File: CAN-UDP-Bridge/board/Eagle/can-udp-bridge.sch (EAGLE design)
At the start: 19 parts, among them IC1 MCP1703DB, IC2 MCP1703DB, Q1 16M, X1 B4B-ZR

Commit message: Added files via upload
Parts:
- removed C4: 100n, rcl:C-EUC0805
- removed C7, C8: 1µ, rcl:C-EUC0805
- removed IC1: MCP1703DB, linear:MCP1703DB
- removed R1: 10kR, rcl:R-EU_R0805
- added U$3: ROF-78E5.0-0.5SMD, ROF-78XX:ROF-78E5.0-0.5SMD
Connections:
- removed net N$12: R1.1, U$1.~RESET
- net +18V: now also U$3.VIN; no longer C8.2, IC1.VI
- net +3V3: no longer R1.2
- net +5V: now also U$3.VOUT; no longer C4.2, C7.2, IC1.VO
- net GND: now also U$3.GND; no longer C4.1, C7.1, C8.1, IC1.GND
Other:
- moved on the sheet: C1, C2, C3, Q1

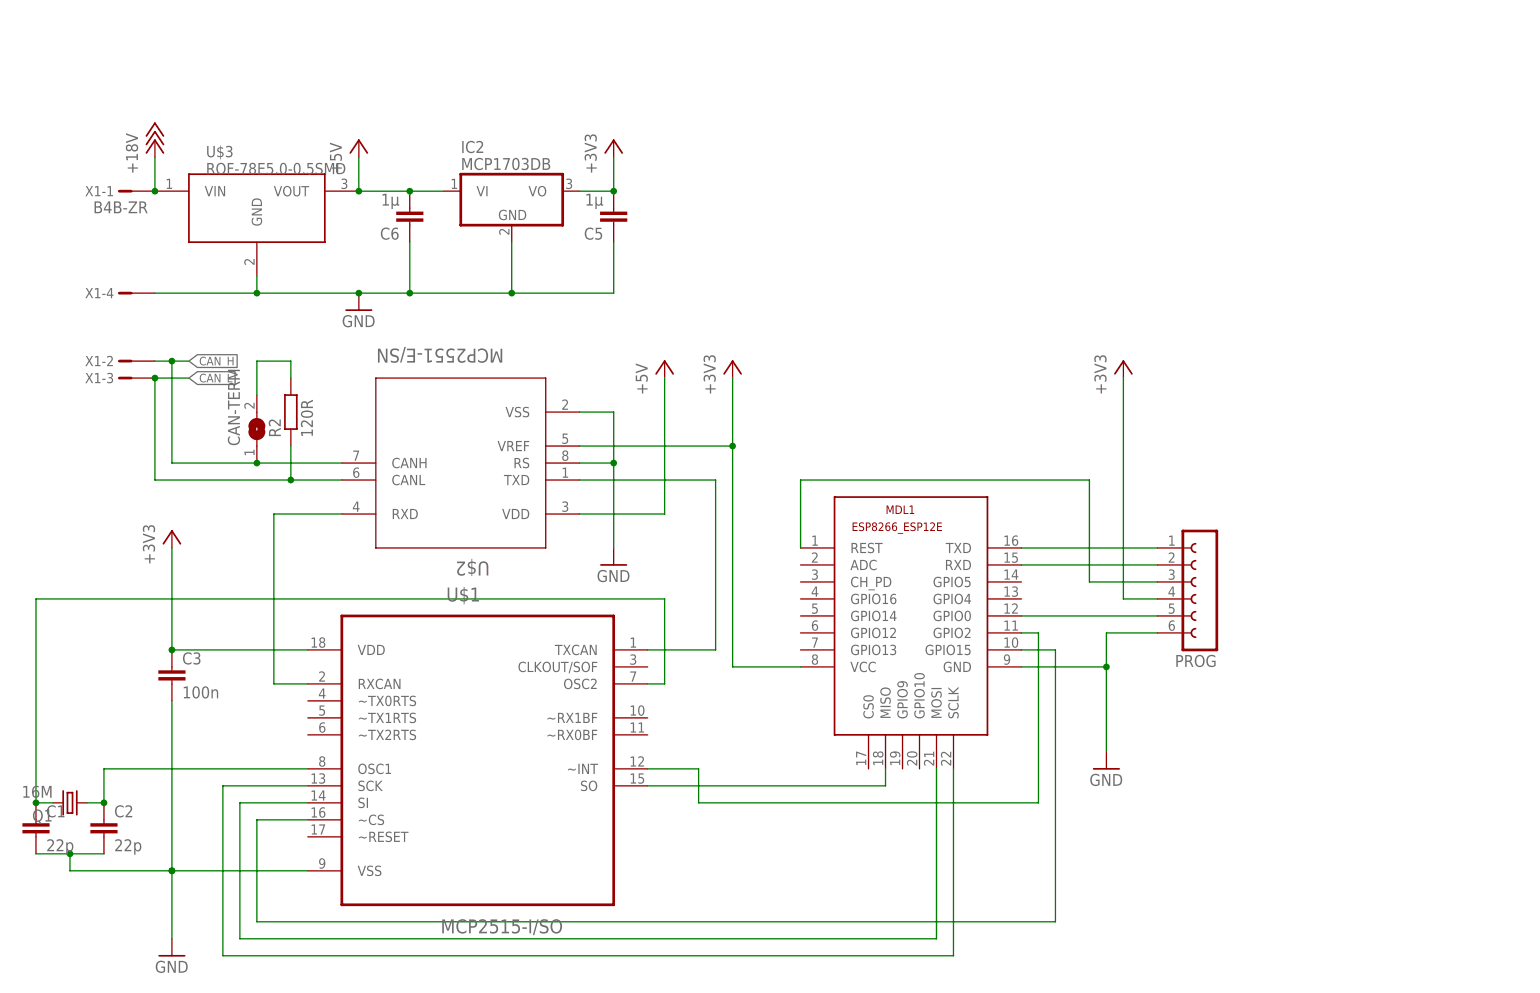
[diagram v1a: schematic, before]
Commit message: Schnittstelle angepasst an FT232RL.
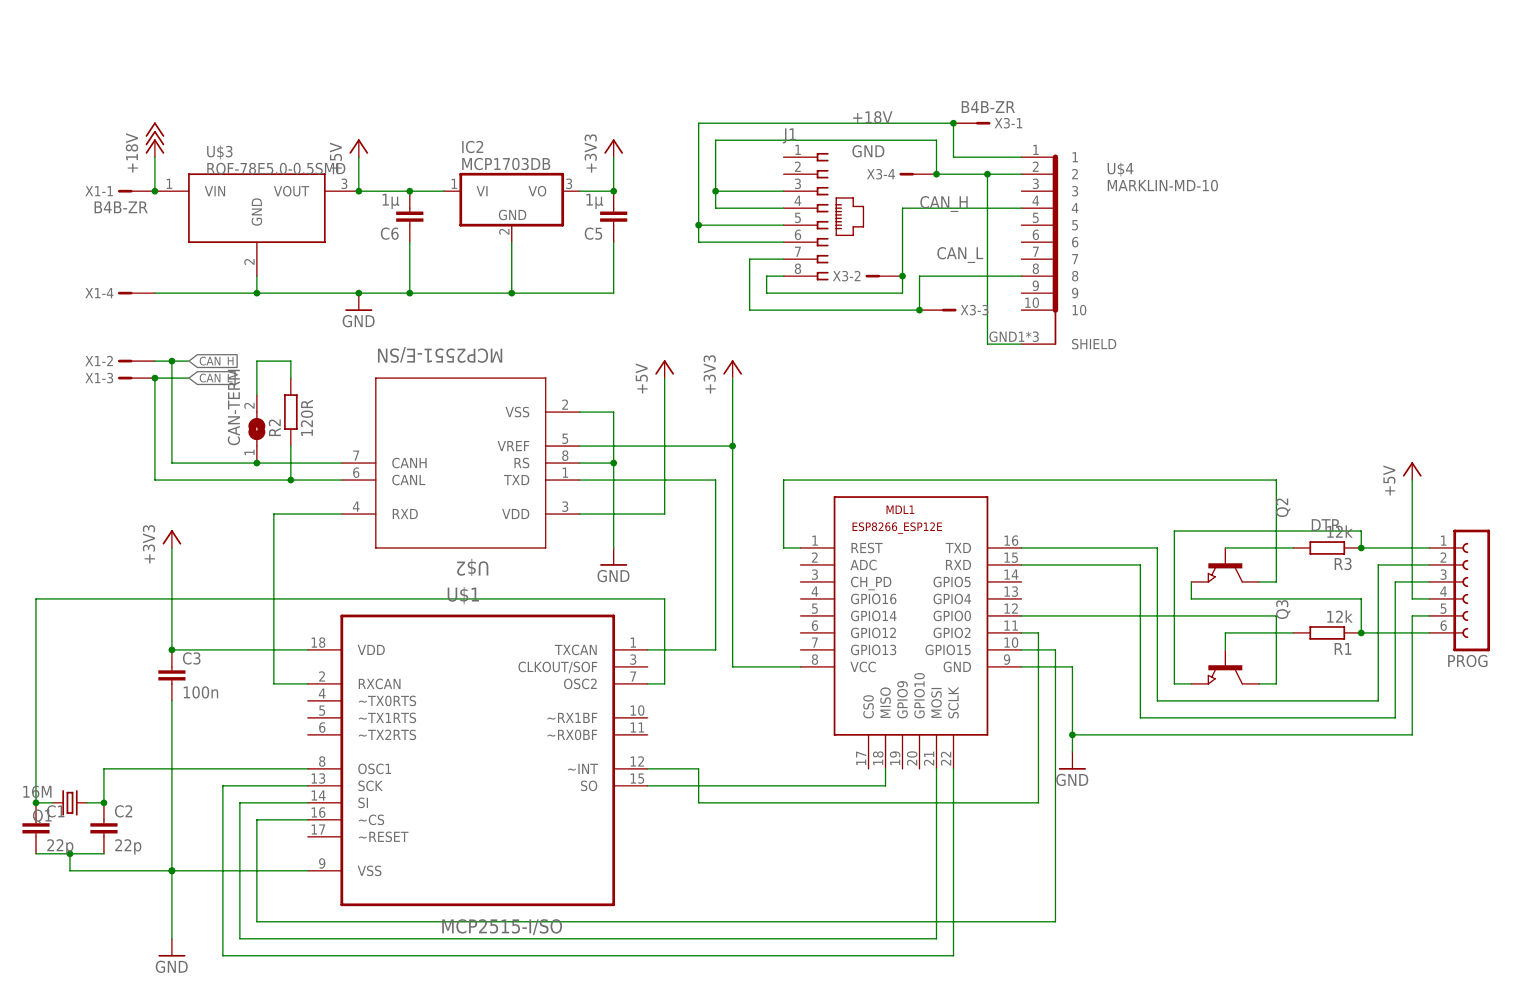
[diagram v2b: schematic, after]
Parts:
- added J1: (no value), con-amp:215877-7
- added Q2, Q3: (no value), semicon-smd-ipc:NPN-TRANSISTOR_SOT23
- added R1, R3: 12k, rcl:R-EU_R0805
- added U$4: MARKLIN-MD-10, Marklin-Mini-DIN:MARKLIN-MD-10
- added X3: B4B-ZR, con-jst:B4B-ZR
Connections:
- new net DTR: PROG.1, Q3.E, R3.1
- new net N$12: Q2.B, R3.2
- new net N$16: MDL1.TXD, PROG.2
- new net N$17: MDL1.RXD, PROG.3
- net +18V: now also J1.5, J1.6, U$4.1, X3-1.1
- net +3V3: no longer PROG.4
- net +5V: now also PROG.4
- net CAN_H: now also J1.8, U$4.4, X3-2.1
- net CAN_L: now also J1.7, U$4.8, X3-3.1
- net GND: now also J1.3, J1.4, PROG.5, U$4.2, U$4.SHIELD, X3-4.1; no longer PROG.6
- net N$10: now also MDL1.GPIO0, Q3.C; no longer MDL1.REST, PROG.3
- net N$11: now also Q3.B, R1.2; no longer MDL1.GPIO0, PROG.5
- net N$3: now also PROG.6, Q2.E, R1.1; no longer MDL1.TXD, PROG.1
- net N$4: now also MDL1.REST, Q2.C; no longer MDL1.RXD, PROG.2
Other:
- moved on the sheet: PROG

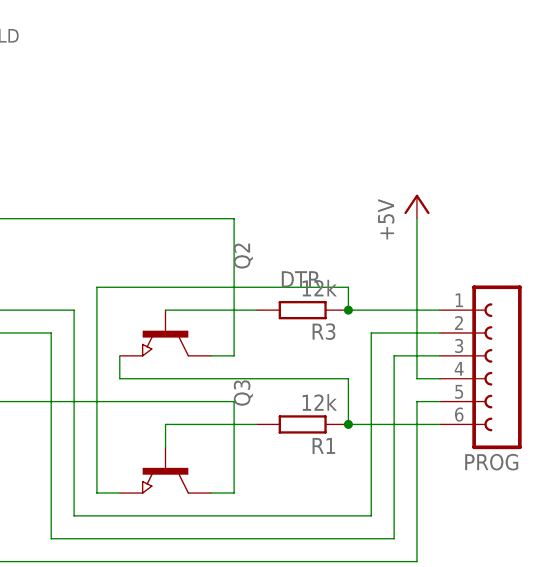
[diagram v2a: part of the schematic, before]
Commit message: Schnittstelle angepasst an FT232RL.
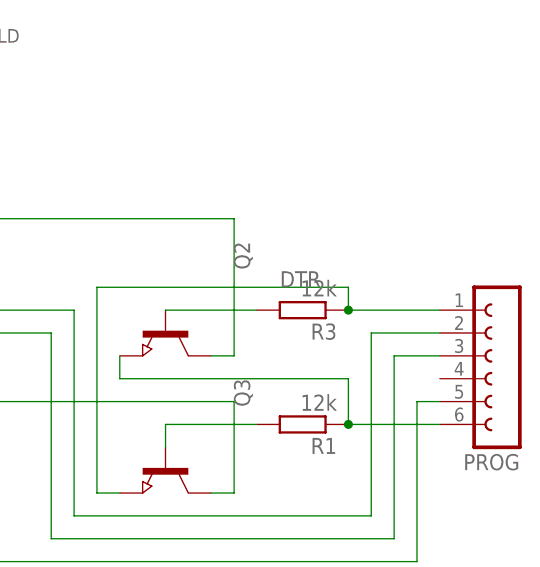
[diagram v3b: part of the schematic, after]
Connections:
- net +5V: no longer PROG.4
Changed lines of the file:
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@@
 <part name="R1" library="rcl" deviceset="R-EU_" device="R0805" value="12k"/>
 <part name="R3" library="rcl" deviceset="R-EU_" device="R0805" value="12k"/>
-<part name="P+4" library="supply1" deviceset="+5V" device=""/>
 </parts>
 <sheets>
@@
 <instance part="R1" gate="G$1" x="208.28" y="10.16" rot="R180"/>
 <instance part="R3" gate="G$1" x="208.28" y="22.86" rot="R180"/>
-<instance part="P+4" gate="1" x="220.98" y="35.56"/>
 </instances>
 <busses>
@@
 <pinref part="P+3" gate="1" pin="+5V"/>
 </segment>
-<segment>
-<pinref part="PROG" gate="G$1" pin="4"/>
-<wire x1="223.52" y1="15.24" x2="220.98" y2="15.24" width="0.1524" layer="91"/>
-<wire x1="220.98" y1="15.24" x2="220.98" y2="33.02" width="0.1524" layer="91"/>
-<pinref part="P+4" gate="1" pin="+5V"/>
-</segment>
 </net>

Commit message: Add files via upload
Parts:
- removed PROG: (no value), con-lsta:FE06W
- added PROG/TTL: (no value), con-lsta:FE06W
- added TRACK: (no value), jumper:JP1E
- U$2: value MCP2551-E/SN -> MCP2562
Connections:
- new net N$18: J1.2, TRACK.2
- new net N$19: J1.1, TRACK.1
- net +3V3: now also MDL1.CH_PD
- net DTR: now also PROG/TTL.1; no longer PROG.1
- net GND: now also PROG/TTL.5; no longer PROG.5
- net N$16: now also PROG/TTL.2; no longer PROG.2
- net N$17: now also PROG/TTL.3; no longer PROG.3
- net N$3: now also PROG/TTL.6; no longer PROG.6
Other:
- moved on the sheet: C5, C6, IC2, J1, U$3, U$4, X1-1, X1-4, X3-1, X3-2, X3-3, X3-4

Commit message: Add files via upload
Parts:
- added C4, C7: 100n, rcl:C-EUC0805
- added R4: 12k, rcl:R-EU_R0805
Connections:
- new net N$20: R4.2, U$1.~RESET
- net +18V: no longer J1.5
- net +3V3: now also C4.2, R4.1
- net +5V: now also C7.1
- net GND: now also C4.1, C7.2; no longer J1.3
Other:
- moved on the sheet: C3
